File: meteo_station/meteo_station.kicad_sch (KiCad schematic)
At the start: 11 parts, among them SW1 SW_SPDT, U1 TP4056, U2 ESP32-WROOM, U3 DS18B20, U4 BH1750, U5 BME280

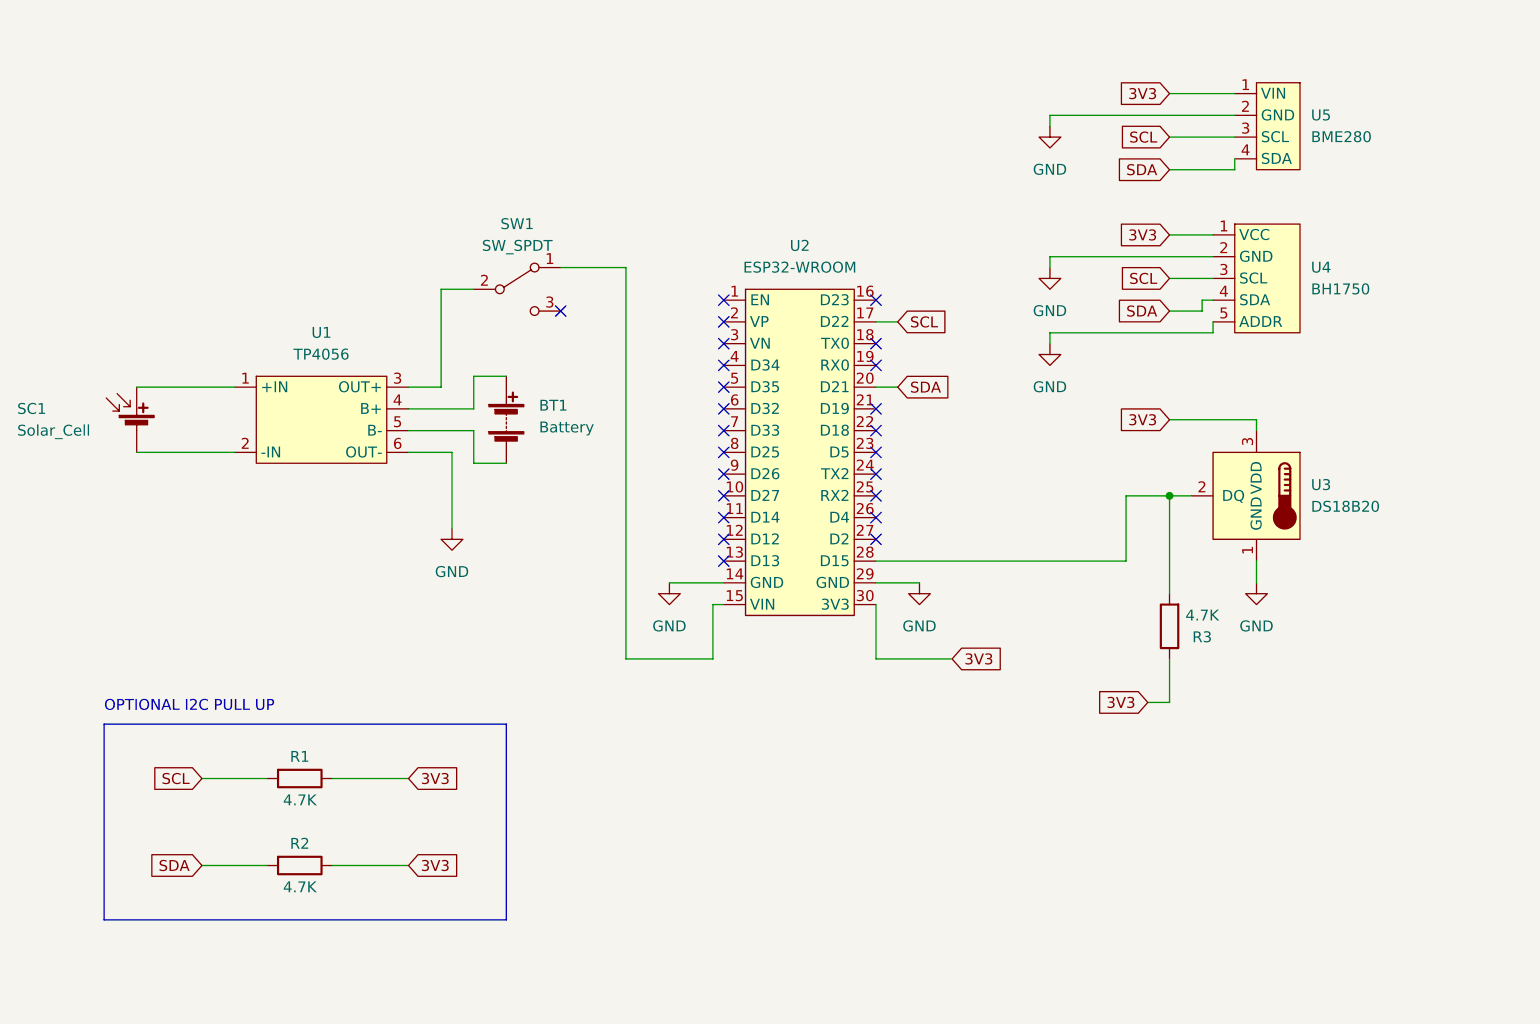
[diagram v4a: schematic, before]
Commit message: Add LDO and battery voltage meter
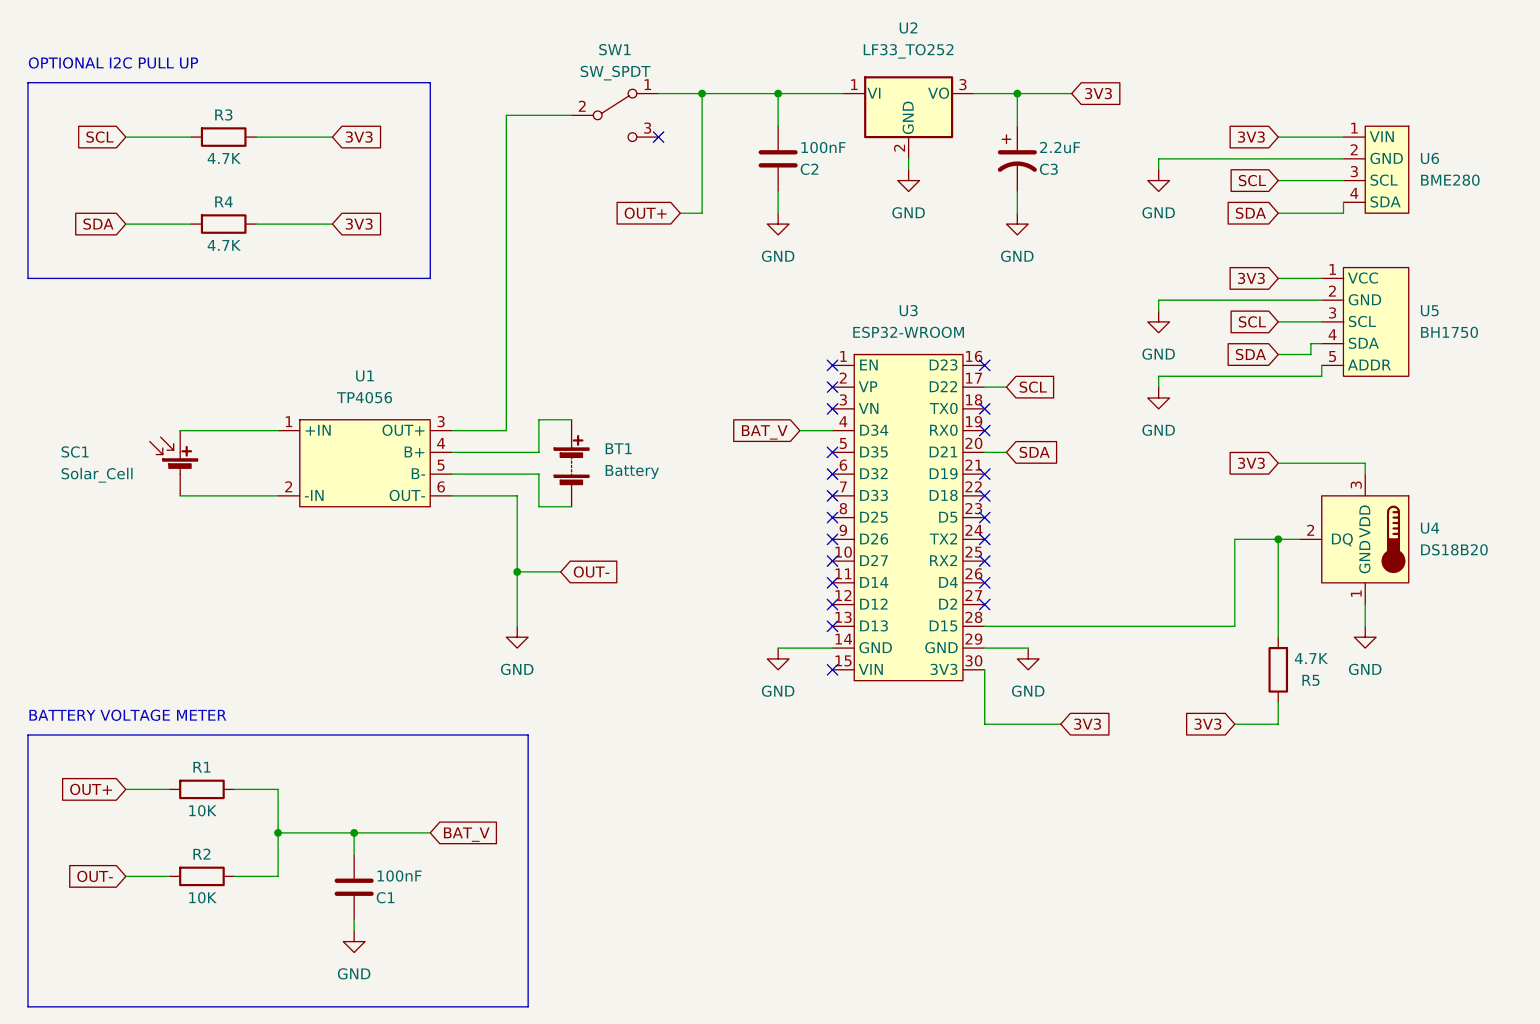
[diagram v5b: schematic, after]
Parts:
- added C1, C2: 100nF, symbol Device:C
- added C3: 2.2uF, symbol Device:C_Polarized_US
- added R1, R2: 10K, Resistor_SMD:R_0603_1608Metric, symbol Device:R
- added U2: LF33_TO252, Package_TO_SOT_SMD:TO-252-2, symbol meteo_station_symbols:LF33_TO252
- renumbered R1 to R3, R2 to R4, R3 to R5, U2 to U3, U3 to U4, U4 to U5, U5 to U6
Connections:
- net 3V3: now also C3.1, U2.3 (VO)
- net GND: now also C1.2, C2.2, C3.2, R2.2, U2.2 (GND)
- net at U3.15 (VIN): no longer SW1.1 (A)
- net BAT_V: now reaches U3.4 (D34)
- net BAT_V: now also C1.1, R1.1, R2.1
- new net OUT+: C2.1, R1.2, SW1.1 (A), U2.1 (VI)
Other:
- note added: "BATTERY VOLTAGE METER"
- moved on the sheet: BT1, R3, R4, R5, SC1, SW1, U1, U3, U4, U5, U6

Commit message: Fix some footprints
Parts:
- removed U2: LF33_TO252, Package_TO_SOT_SMD:TO-252-2, symbol meteo_station_symbols:LF33_TO252
- added U2: LF33_TO220, Package_TO_SOT_THT:TO-220-3_Vertical, symbol meteo_station_symbols:LF33_TO220
- BT1: footprint Battery:BatteryHolder_MPD_BH-18650-PC2 -> meteo_station_footprints:BatteryHolder
- C1, C2: footprint (none) -> Capacitor_SMD:C_0603_1608Metric
- C3: footprint (none) -> Capacitor_Tantalum_SMD:CP_EIA-3216-18_Kemet-A
- SC1: footprint meteo_station_footprints:SolarPanel -> meteo_station_footprints:SolarPanel_JST
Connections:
- net 3V3: now also U2.3 (VO)
- net GND: now also U2.2 (GND)
- net OUT+: now also U2.1 (VI)
- net at U3.26 (D4): now also R5.2, U4.2 (DQ)
- now unconnected: U3.28 (D15)
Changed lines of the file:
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@@
   (no_connect (at 111.76 66.04))
   (no_connect (at 111.76 68.58))
-  (no_connect (at 129.54 81.28))
+  (no_connect (at 129.54 86.36))
   (polyline (pts (xy 17.78 22.86) (xy 17.78 45.72))
     (stroke (width 0) (type default) (color 0 0 0 0))
   )
-  (wire (pts (xy 158.75 76.2) (xy 158.75 86.36))
+  (wire (pts (xy 158.75 76.2) (xy 158.75 81.28))
     (stroke (width 0) (type default) (color 0 0 0 0))
   )
@@
     (stroke (width 0) (type default) (color 0 0 0 0))
   )
-  (wire (pts (xy 129.54 86.36) (xy 158.75 86.36))
-    (stroke (width 0) (type default) (color 0 0 0 0))
-  )
   (wire (pts (xy 81.28 72.39) (xy 77.47 72.39))
     (stroke (width 0) (type default) (color 0 0 0 0))
@@
   )
   (wire (pts (xy 133.35 35.56) (xy 133.35 38.1))
+    (stroke (width 0) (type default) (color 0 0 0 0))
+  )
+  (wire (pts (xy 129.54 81.28) (xy 158.75 81.28))
     (stroke (width 0) (type default) (color 0 0 0 0))
   )
@@
       (effects (font (size 1.27 1.27)) (justify left))
     )
-    (property "Footprint" "" (id 2) (at 56.8452 120.65 0)
+    (property "Footprint" "Capacitor_SMD:C_0603_1608Metric" (id 2) (at 56.8452 120.65 0)
       (effects (font (size 1.27 1.27)) hide)
     )
@@
       (effects (font (size 1.27 1.27)) (justify left))
     )
-    (property "Footprint" "Battery:BatteryHolder_MPD_BH-18650-PC2" (id 2) (at 81.28 65.786 90)
+    (property "Footprint" "meteo_station_footprints:BatteryHolder" (id 2) (at 81.28 65.786 90)
       (effects (font (size 1.27 1.27)) hide)
     )
@@
     )
     (pin "1")
-  )
-  (symbol (lib_id "meteo_station_symbols:LF33_TO252") (at 120.65 24.13 0) (unit 1)
-    (in_bom yes) (on_board yes) (fields_autoplaced)
-    (property "Reference" "U2" (id 0) (at 120.65 16.51 0))
-    (property "Value" "LF33_TO252" (id 1) (at 120.65 19.05 0))
-    (property "Footprint" "Package_TO_SOT_SMD:TO-252-2" (id 2) (at 120.65 18.415 0)
-      (effects (font (size 1.27 1.27) italic) hide)
-    )
-    (property "Datasheet" "http://www.st.com/content/ccc/resource/technical/document/datasheet/c4/0e/7e/2a/be/bc/4c/bd/CD00000546.pdf/files/CD00000546.pdf/jcr:content/translations/en.CD00000546.pdf" (id 3) (at 120.65 25.4 0)
-      (effects (font (size 1.27 1.27)) hide)
-    )
-    (pin "1")
-    (pin "2")
-    (pin "3")
   )
   (symbol (lib_id "power:GND") (at 149.86 49.53 0) (unit 1)
@@
     (pin "1")
   )
+  (symbol (lib_id "meteo_station_symbols:LF33_TO220") (at 120.65 24.13 0) (unit 1)
+    (in_bom yes) (on_board yes) (fields_autoplaced)
+    (property "Reference" "U2" (id 0) (at 120.65 17.78 0))
+    (property "Value" "LF33_TO220" (id 1) (at 120.65 20.32 0))
+    (property "Footprint" "Package_TO_SOT_THT:TO-220-3_Vertical" (id 2) (at 120.65 18.415 0)
+      (effects (font (size 1.27 1.27) italic) hide)
+    )
+    (property "Datasheet" "http://www.st.com/content/ccc/resource/technical/document/datasheet/c4/0e/7e/2a/be/bc/4c/bd/CD00000546.pdf/files/CD00000546.pdf/jcr:content/translations/en.CD00000546.pdf" (id 3) (at 120.65 25.4 0)
+      (effects (font (size 1.27 1.27)) hide)
+    )
+    (pin "1")
+    (pin "2")
+    (pin "3")
+  )
   (symbol (lib_id "Device:C") (at 105.41 31.75 0) (unit 1)
     (in_bom yes) (on_board yes)
@@
       (effects (font (size 1.27 1.27)) (justify left))
     )
-    (property "Footprint" "" (id 2) (at 106.3752 35.56 0)
+    (property "Footprint" "Capacitor_SMD:C_0603_1608Metric" (id 2) (at 106.3752 35.56 0)
       (effects (font (size 1.27 1.27)) hide)
     )
@@
       (effects (font (size 1.27 1.27)) (justify left))
     )
-    (property "Footprint" "" (id 2) (at 133.35 31.75 0)
+    (property "Footprint" "Capacitor_Tantalum_SMD:CP_EIA-3216-18_Kemet-A" (id 2) (at 133.35 31.75 0)
       (effects (font (size 1.27 1.27)) hide)
     )
@@
       (effects (font (size 1.27 1.27)) (justify left))
     )
-    (property "Footprint" "meteo_station_footprints:SolarPanel" (id 2) (at 35.56 67.056 90)
+    (property "Footprint" "meteo_station_footprints:SolarPanel_JST" (id 2) (at 35.56 67.056 90)
       (effects (font (size 1.27 1.27)) hide)
     )
@@
     )
     (path "/a7c72c64-c327-4ae9-9904-b1572c7f32f2"
-      (reference "BT1") (unit 1) (value "Battery") (footprint "Battery:BatteryHolder_MPD_BH-18650-PC2")
+      (reference "BT1") (unit 1) (value "Battery") (footprint "meteo_station_footprints:BatteryHolder")
     )
     (path "/873564cb-cd94-41ff-aeb6-67ea49c79a1a"
-      (reference "C1") (unit 1) (value "100nF") (footprint "")
+      (reference "C1") (unit 1) (value "100nF") (footprint "Capacitor_SMD:C_0603_1608Metric")
     )
     (path "/d543dfc1-54f5-4cb4-8bb6-ce43b71bd997"
-      (reference "C2") (unit 1) (value "100nF") (footprint "")
+      (reference "C2") (unit 1) (value "100nF") (footprint "Capacitor_SMD:C_0603_1608Metric")
     )
     (path "/df8a65c6-b707-4335-b81d-c6c76ba9cfff"
-      (reference "C3") (unit 1) (value "2.2uF") (footprint "")
+      (reference "C3") (unit 1) (value "2.2uF") (footprint "Capacitor_Tantalum_SMD:CP_EIA-3216-18_Kemet-A")
     )
     (path "/ea78ddbc-2970-428e-b50b-675425fbb699"
@@
     )
     (path "/e3bc8b35-8aa9-44ed-b10b-bbd343541f80"
-      (reference "SC1") (unit 1) (value "Solar_Cell") (footprint "meteo_station_footprints:SolarPanel")
+      (reference "SC1") (unit 1) (value "Solar_Cell") (footprint "meteo_station_footprints:SolarPanel_JST")
     )
     (path "/a30bd64c-5664-40ec-b5dc-e115cbdaa123"
@@
       (reference "U1") (unit 1) (value "TP4056") (footprint "meteo_station_footprints:TP4056")
     )
-    (path "/be865c6e-cd05-4b55-8da4-bb7b2ca8120d"
-      (reference "U2") (unit 1) (value "LF33_TO252") (footprint "Package_TO_SOT_SMD:TO-252-2")
+    (path "/cd3aea37-37f7-4673-bd53-2b06ffe90909"
+      (reference "U2") (unit 1) (value "LF33_TO220") (footprint "Package_TO_SOT_THT:TO-220-3_Vertical")
     )
     (path "/93a49863-00ee-408b-9e67-37bd2abd68da"

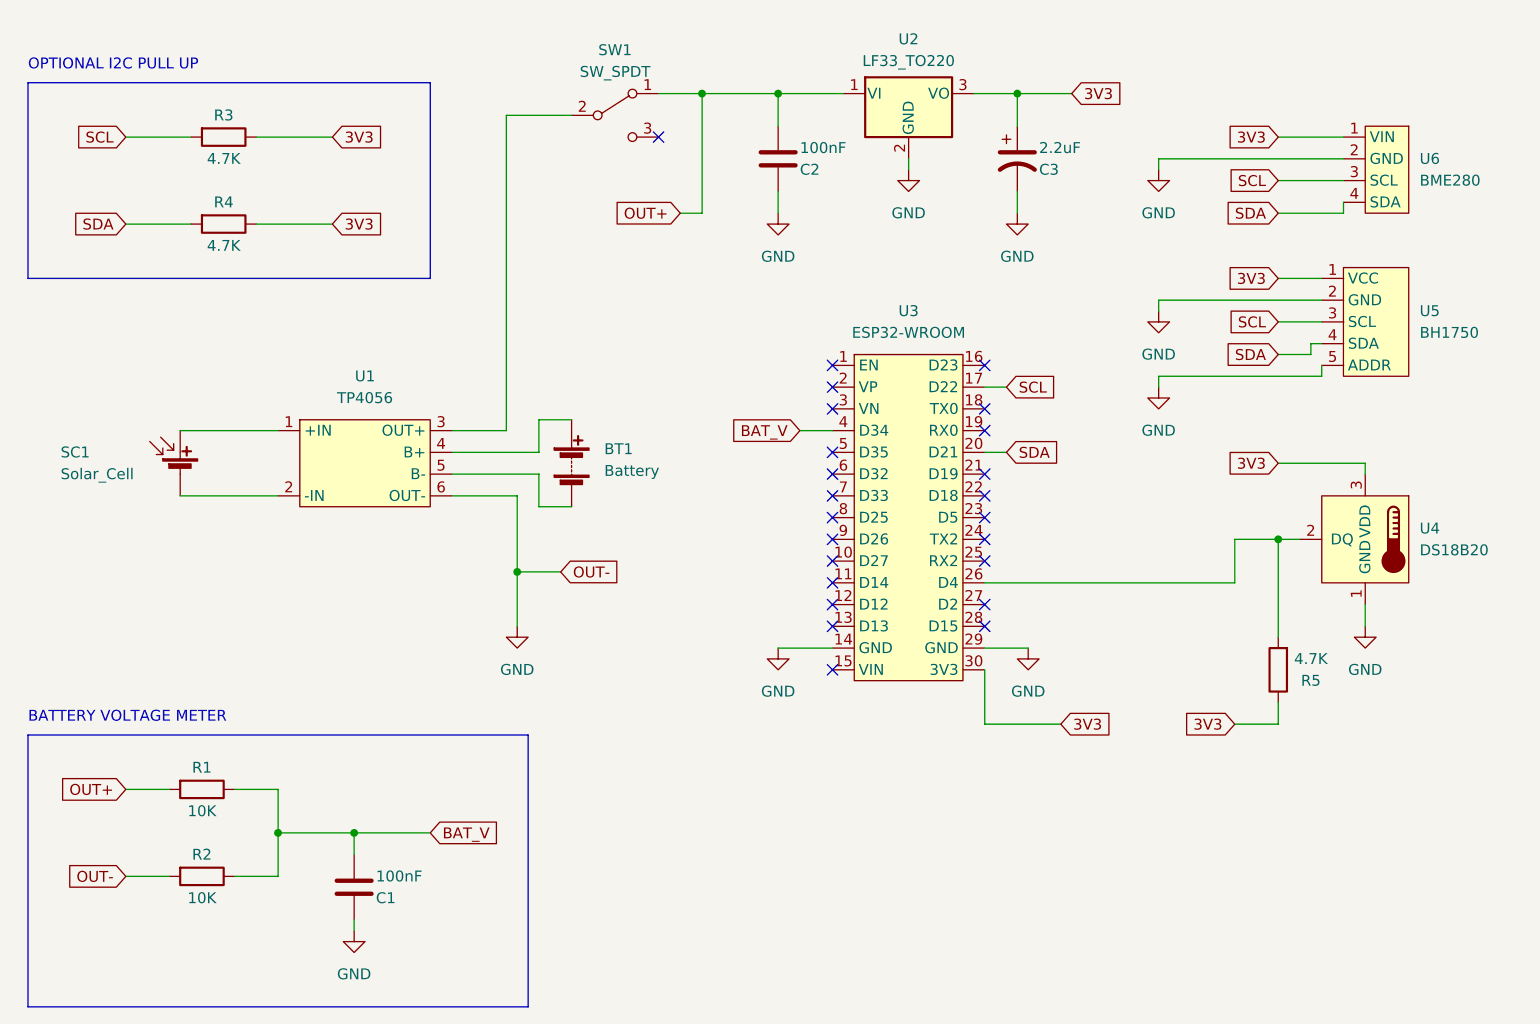
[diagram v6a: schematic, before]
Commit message: Add second solar panel
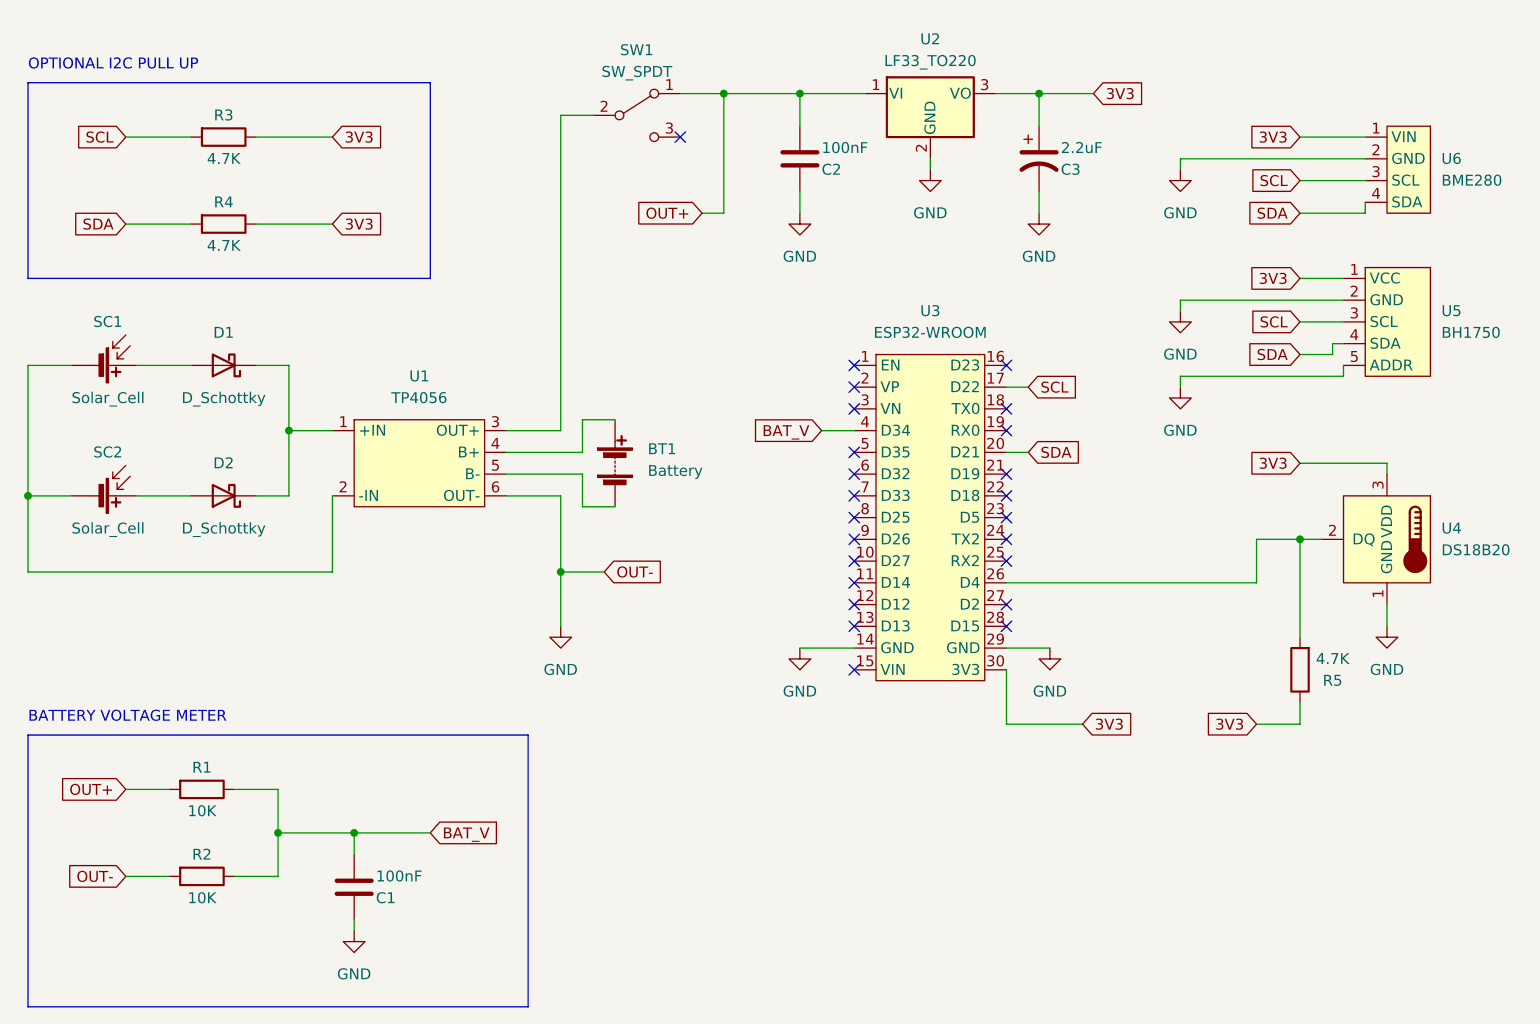
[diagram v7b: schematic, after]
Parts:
- added D1, D2: D_Schottky, Diode_SMD:D_SMB_Handsoldering, symbol Device:D_Schottky
- added SC2: Solar_Cell, meteo_station_footprints:SolarPanel_JST, symbol Device:Solar_Cell
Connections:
- net at U1.1 (+IN): now also D1.1 (K), D2.1 (K); no longer SC1.1 (+)
- net at SC1.2 (-), U1.2 (-IN): now also SC2.2 (-)
- new net: D2.2 (A), SC2.1 (+)
- new net: D1.2 (A), SC1.1 (+)
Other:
- moved on the sheet: BT1, C2, C3, R5, SW1, U1, U2, U3, U4, U5, U6

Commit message: Update termometer footprint
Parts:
- U4: footprint Package_TO_SOT_THT:TO-92_Inline -> meteo_station_footprints:TO-92_Inline
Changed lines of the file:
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@@
       (effects (font (size 1.27 1.27)) (justify right))
     )
-    (property "Footprint" "Package_TO_SOT_THT:TO-92_Inline" (id 2) (at 201.93 82.55 0)
+    (property "Footprint" "meteo_station_footprints:TO-92_Inline" (id 2) (at 201.93 82.55 0)
       (effects (font (size 1.27 1.27)) hide)
     )
@@
     )
     (path "/dfceaf99-0117-4f2d-8240-339c614bf0fc"
-      (reference "U4") (unit 1) (value "DS18B20") (footprint "Package_TO_SOT_THT:TO-92_Inline")
+      (reference "U4") (unit 1) (value "DS18B20") (footprint "meteo_station_footprints:TO-92_Inline")
     )
     (path "/ed6dd4e3-cfe6-415c-94e1-38553a3a4527"
